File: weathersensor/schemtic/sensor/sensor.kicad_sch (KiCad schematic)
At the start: 1 part

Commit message: backup
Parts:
- removed J?: Conn_Coaxial, symbol Connector:Conn_Coaxial
- added C1, C2, C? (x3): 1.0u, symbol Device:C_Small
- added C3: 10u, symbol Device:C_Small
- added C? (x2): C_Polarized, symbol Device:C_Polarized
- added D1: BAT60A, Diode_SMD:D_SOD-323, symbol Diode:BAT60A
- added D2, D? (x2): LED, symbol Device:LED
- added D? (x2): D_Schottky, symbol Device:D_Schottky
- added IC?: CN3791, SSOP10, symbol CN3791:CN3791
- added J1: Conn_01x04_Male, Connector_JST:JST_XH_B4B-XH-AM_1x04_P2.50mm_Vertical, symbol Connector:Conn_01x04_Male
- added J2: Conn_01x02_Male, Connector_JST:JST_PH_B2B-PH-K_1x02_P2.00mm_Vertical, symbol Connector:Conn_01x02_Male
- added J3: Conn_01x02_Male, Connector_JST:JST_XH_B2B-XH-AM_1x02_P2.50mm_Vertical, symbol Connector:Conn_01x02_Male
- added L?: INDUCTOR, symbol pspice:INDUCTOR
- added Q1: IRLML6401, Package_TO_SOT_SMD:SOT-23, symbol Transistor_FET:IRLML6401
- added R1, R2: 10k, symbol Device:R
- added R3, R? (x4): 1k, symbol Device:R
- added U1: XC6220B331MR, Package_TO_SOT_SMD:SOT-23-5, symbol Regulator_Linear:XC6220B331MR
- added U2: CH340C, Package_SO:SOIC-16_3.9x9.9mm_P1.27mm, symbol Interface_USB:CH340C
- added U3: MS5611-01BA, Package_LGA:LGA-8_3x5mm_P1.25mm, symbol Sensor_Pressure:MS5611-01BA
- added U4: RFM95W-868S2, RF_Module:HOPERF_RFM9XW_THT, symbol RF_Module:RFM95W-868S2
- added U6: MAX17048G, SON50P200X200X80-9N, symbol MAX17048G:MAX17048G
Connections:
- new net: C1.1, D1.1 (K), Q1.2 (S), R2.1, U1.1 (VIN)
- new net: R2.2, U1.3 (CE)
- new net: D2.2 (A), R3.2
- new net: U3.4 (CSB), U3.5 (CSB)
- new net +3.3V: C2.1, C3.1, R3.1, U1.5 (VOUT)
- new net GND: C1.2, C2.2, C3.2, D2.1 (K), R1.2, U1.2 (GND)
- new net VSS: C?.1
- new net V_BAT: Q1.3 (D)
- new net V_USB: D1.2 (A), Q1.1 (G), R1.1
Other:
- note added: "Power Supply"

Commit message: Start commit message
21.03.2023
	- create and pcb for weathersensor

22.02.2023
	- add schematic and pcb for mqtt_wlan_bridge
	- remove old from git repo

	TODO:
	- create schematic and pcb for weathersensor
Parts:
- removed D? (x2): LED, symbol Device:LED
- removed R?: 1k, symbol Device:R
- added C11, C13, C8: 100n, Capacitor_SMD:C_1206_3216Metric, symbol Device:C_Small
- added C12: 1u, Capacitor_SMD:C_1206_3216Metric, symbol Device:C_Small
- added C7: 22n, Capacitor_SMD:C_1206_3216Metric, symbol Device:C_Small
- added IC2: DW01A, DW01A:SOT23-6, symbol DW01A:DW01A
- added J4: ANT, Connector_Coaxial:SMA_Amphenol_901-144_Vertical, symbol Connector:Conn_Coaxial
- added P1: USB_C_Plug_USB2.0, Connector_USB:USB_C_Receptacle_HRO_TYPE-C-31-M-12, symbol Connector:USB_C_Plug_USB2.0
- added Q2: AO3401A, Package_TO_SOT_SMD:SOT-23, symbol Transistor_FET:AO3401A
- added Q3: FS8205, FS8205:SOT95P280X145-6N, symbol FS8205:FS8205
- added Q4, Q5: BSS138, Package_TO_SOT_SMD:SOT-23, symbol Transistor_FET:BSS138
- added R10: 1k, Resistor_SMD:R_1206_3216Metric, symbol Device:R
- added R11, R4: 5k1, Resistor_SMD:R_1206_3216Metric, symbol Device:R
- added R12, R13: 10k, Resistor_SMD:R_1206_3216Metric, symbol Device:R
- added R7: 178k, Resistor_SMD:R_1206_3216Metric, symbol Device:R
- added R8: 100, Resistor_SMD:R_1206_3216Metric, symbol Device:R
- C1, C2: footprint (none) -> Capacitor_SMD:C_1206_3216Metric; Feld4 (none) -> C107185
- C10: renamed from C?; value 1.0u -> 220n; footprint (none) -> Capacitor_SMD:C_1206_3216Metric; Feld4 (none) -> C377090
- C3: footprint (none) -> Capacitor_SMD:C_1206_3216Metric; Feld4 (none) -> C92797
- C4, C9: renamed from C?; value C_Polarized -> 47u/16V; footprint (none) -> Capacitor_SMD:CP_Elec_5x5.3; Feld4 (none) -> C134798
- C5: renamed from C?; value 1.0u -> 10n; footprint (none) -> Capacitor_SMD:C_1206_3216Metric; Feld4 (none) -> C1846
- C6: renamed from C?; value 1.0u -> 100n; footprint (none) -> Capacitor_SMD:C_1206_3216Metric; Feld4 (none) -> C377067
- D1: Feld4 (none) -> C117485
- D2: footprint (none) -> LED_SMD:LED_1206_3216Metric; Feld4 (none) -> C84273
- D5, D6: renamed from D?; value D_Schottky -> SSB43L; footprint (none) -> Diode_SMD:D_SMB; Feld4 (none) -> C222519
- IC1: renamed from IC?; footprint SSOP10 -> CN3791:SSOP10; Feld4 (none) -> C154992
- J1: value Conn_01x04_Male -> I2C
- J2: value Conn_01x02_Male -> PANEL; footprint Connector_JST:JST_PH_B2B-PH-K_1x02_P2.00mm_Vertical -> TerminalBlock:TerminalBlock_Altech_AK300-2_P5.00mm
- J3: value Conn_01x02_Male -> BAT
- L1: renamed from L?; value INDUCTOR -> 82u; footprint (none) -> Inductor_SMD:L_12x12mm_H8mm; Feld4 (none) -> C504035
- Q1: Feld4 (none) -> C347501
- R1, R2: footprint (none) -> Resistor_SMD:R_1206_3216Metric; Feld4 (none) -> C118075
- R3: footprint (none) -> Resistor_SMD:R_1206_3216Metric; Feld4 (none) -> C4410
- R5: renamed from R?; value 1k -> 120; footprint (none) -> Resistor_SMD:R_1206_3216Metric; Feld4 (none) -> C114928
- R6: renamed from R?; value 1k -> 22k; footprint (none) -> Resistor_SMD:R_1206_3216Metric; Feld4 (none) -> C25830
- R9: renamed from R?; value 1k -> 0.05; footprint (none) -> Resistor_SMD:R_1206_3216Metric; Feld4 (none) -> C149662
- U1: Feld4 (none) -> C86534
- U2: Feld4 (none) -> C84681
- U3: Feld4 (none) -> C37148
- U6: footprint SON50P200X200X80-9N -> MAX17048G:SON50P200X200X80-9N; Feld4 (none) -> C2682616
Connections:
- net +3.3V: now also J1.1 (Pin_1), U2.16 (VCC), U2.4 (V3), U3.1 (VDD), U3.2 (PS), U4.13 (3.3V), C11.1, C13.1, R12.2, R13.2
- net GND: now also C1.1, C10.2, C4.2, C5.2, C9.2, D6.2 (A), IC1.2 (GND), J1.2 (Pin_2), J2.2 (Pin_2), J3.2 (Pin_2), R6.1, U2.1 (GND), U3.3 (GND), U3.4 (CSB), U3.5 (CSB), U4.1 (GND), U4.10 (GND), U4.8 (GND), U6.1 (CTG), U6.4 (GND), U6.6 (QSTRT), C11.2, C12.2, C13.2, C7.2, C8.2, IC2.6 (GND), J4.2 (Ext), P1.A1 (GND), P1.A12 (GND), P1.B1 (GND), P1.B12 (GND), P1.S1 (SHIELD), Q3.3, R10.1, R11.1, R4.1; no longer C1.2
- net VSS: now also C4.1, C5.1, IC1.9 (VCC), J2.1 (Pin_1), Q2.3 (D), Q3.1, R7.2
- net V_BAT: now also C10.1, C9.1, J3.1 (Pin_1), R9.2, U6.2 (CELL), U6.3 (VDD), R8.2
- net V_USB: now also P1.A4 (VBUS), P1.A9 (VBUS), P1.B4 (VBUS), P1.B9 (VBUS)
- net SCL: now reaches J1.3 (Pin_3)
- net SCL: now also U3.8 (SCLK), U6.7 (SCL), R12.1
- net SDA: now reaches J1.4 (Pin_4)
- net SDA: now also U3.7 (SDI/SDA), U6.8 (SDA), R13.1
- net at D1.1 (K), Q1.2 (S), R2.1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: now also C1.2; no longer C1.1
- net at C6.2: now also IC1.1 (VG)
- net at R5.1: now also IC1.5 (COM)
- net at R5.2: now also C7.1
- net RFM_DI0: now reaches U4.14 (DIO0)
- net MISO: now reaches U4.2 (MISO)
- net MOSI: now reaches U4.3 (MOSI)
- net SCK: now reaches U4.4 (SCK)
- net RFM_SS: now reaches U4.5 (NSS)
- net RFM_RESET: now reaches U4.6 (RESET)
- net RF_ANT: now reaches U4.9 (ANT)
- net RF_ANT: now also J4.1 (In)
- net at R9.1: now also IC1.7 (BAT), L1.2
- net at D6.1 (K): now also D5.1 (K), IC1.8 (CSP), L1.1
- net at R6.2: now also IC1.6 (MPPT), R7.1
- net at IC1.10 (DRV): now also Q2.1 (G)
- net CHARGE: now reaches IC1.3 (CHRG)
- net CRG_DONE: now reaches IC1.4 (DONE)
- net at U2.13 (~{DTR}): now also Q4.1 (G), Q5.2 (S)
- net at U2.14 (~{RTS}): now also Q4.2 (S), Q5.1 (G)
- net ESP32_RX: now reaches U2.2 (TXD)
- net ESP32_TX: now reaches U2.3 (RXD)
- net at U2.5 (UD+): now also P1.A6 (D+)
- net at U2.6 (UD-): now also P1.A7 (D-)
- net at D5.2 (A): now also Q2.2 (S)
- net ALERT: now reaches U6.5 (~{ALERT})
- new net: IC2.2 (CS), R10.2
- new net: C8.1, IC2.5 (VCC), R8.1
- new net: Q3.2, Q3.5
- new net: IC2.3 (OC), Q3.4
- new net: IC2.1 (OD), Q3.6
- new net: P1.A5 (CC), R11.2
- new net: P1.B5 (VCONN), R4.2
- new net ESP32_EN: C12.1, Q4.3 (D)
- new net ESP32_IO0: Q5.3 (D)
- no-connect marks 0 -> 14
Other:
- added sheet ESP32_WROOM (untitled.kicad_sch)
- note added: "Barometer"
- note added: "Fuel Gauge"
- note added: "I2C Address 0x77"
- note added: "LiPo Proctection"
- note added: "LiPo-Charger"
- title: (none) -> Ambiente Sensor
- moved on the sheet: C1, C10, C4, C5, C6, C9, D5, D6, IC1, J1, J2, J3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

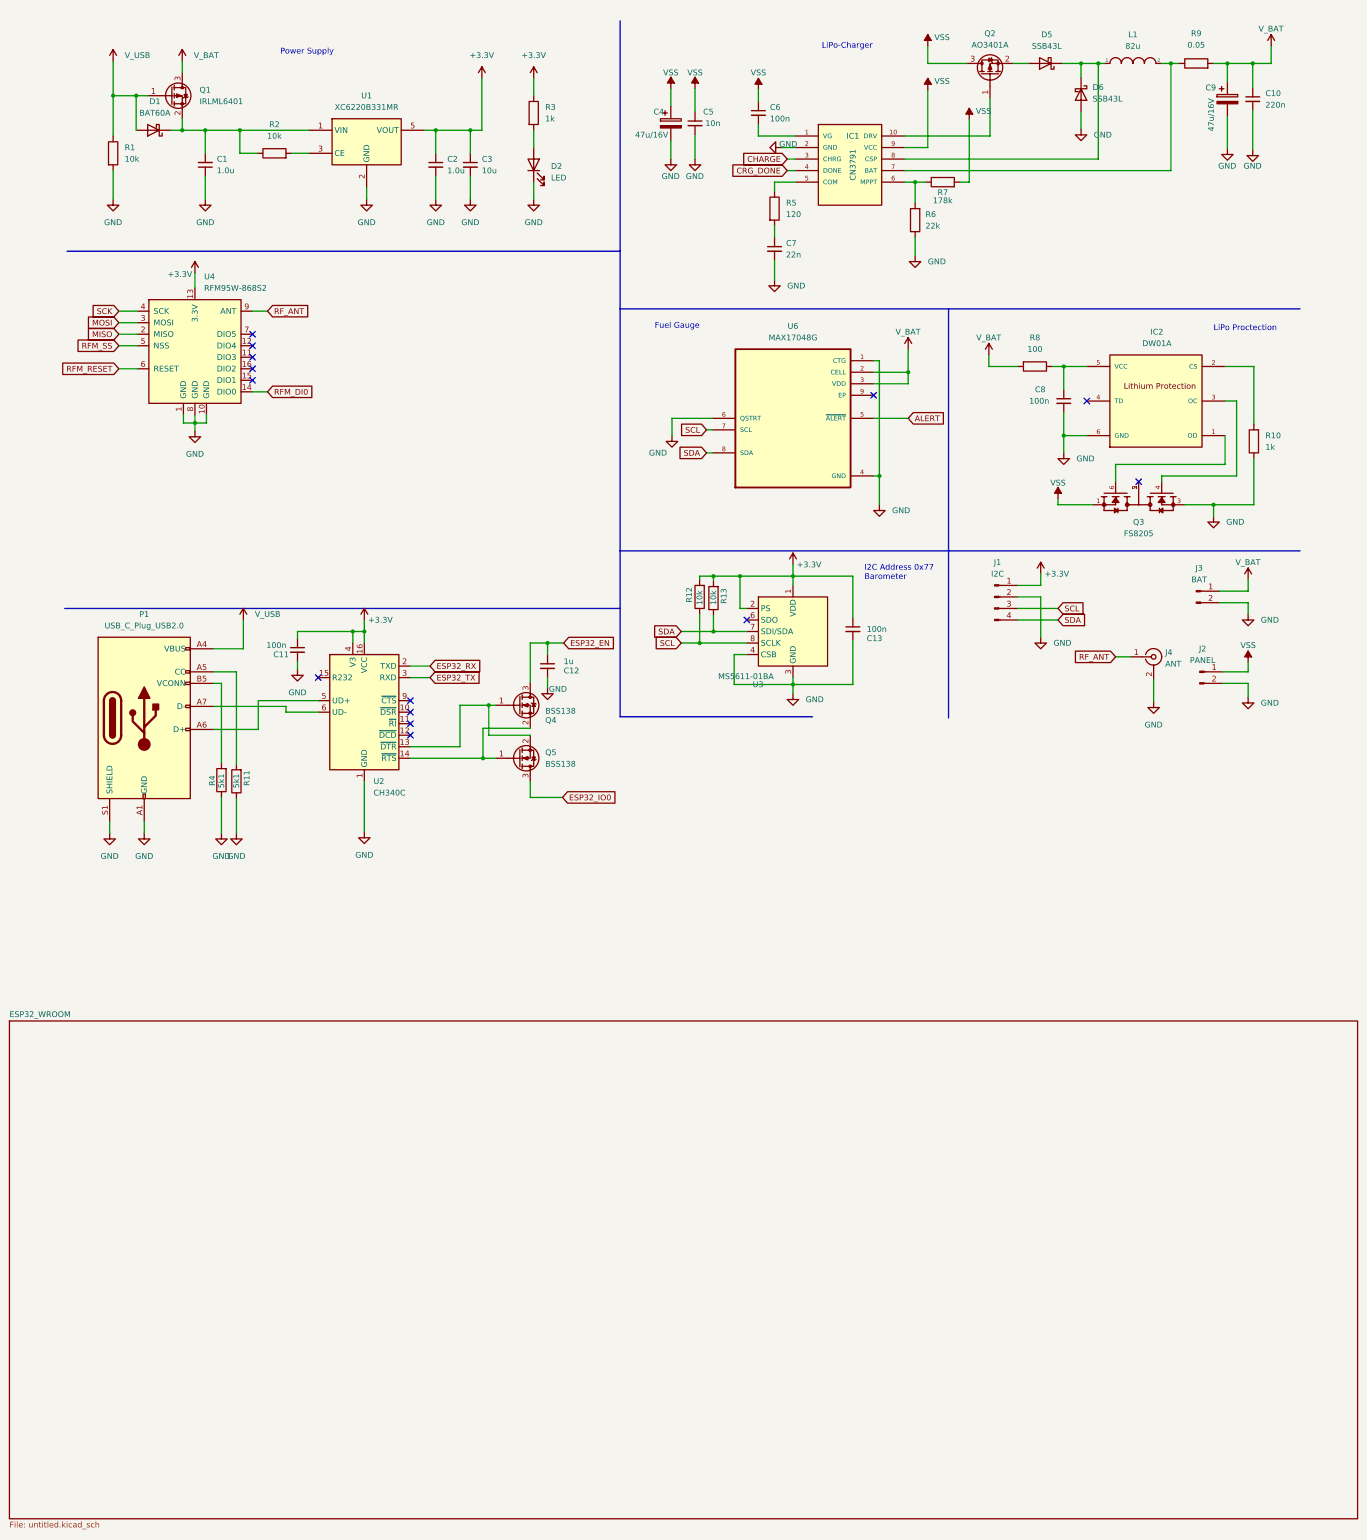
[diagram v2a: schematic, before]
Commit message: Changes in Source Code:
    use the interal ADC for measure battery and panel voltage
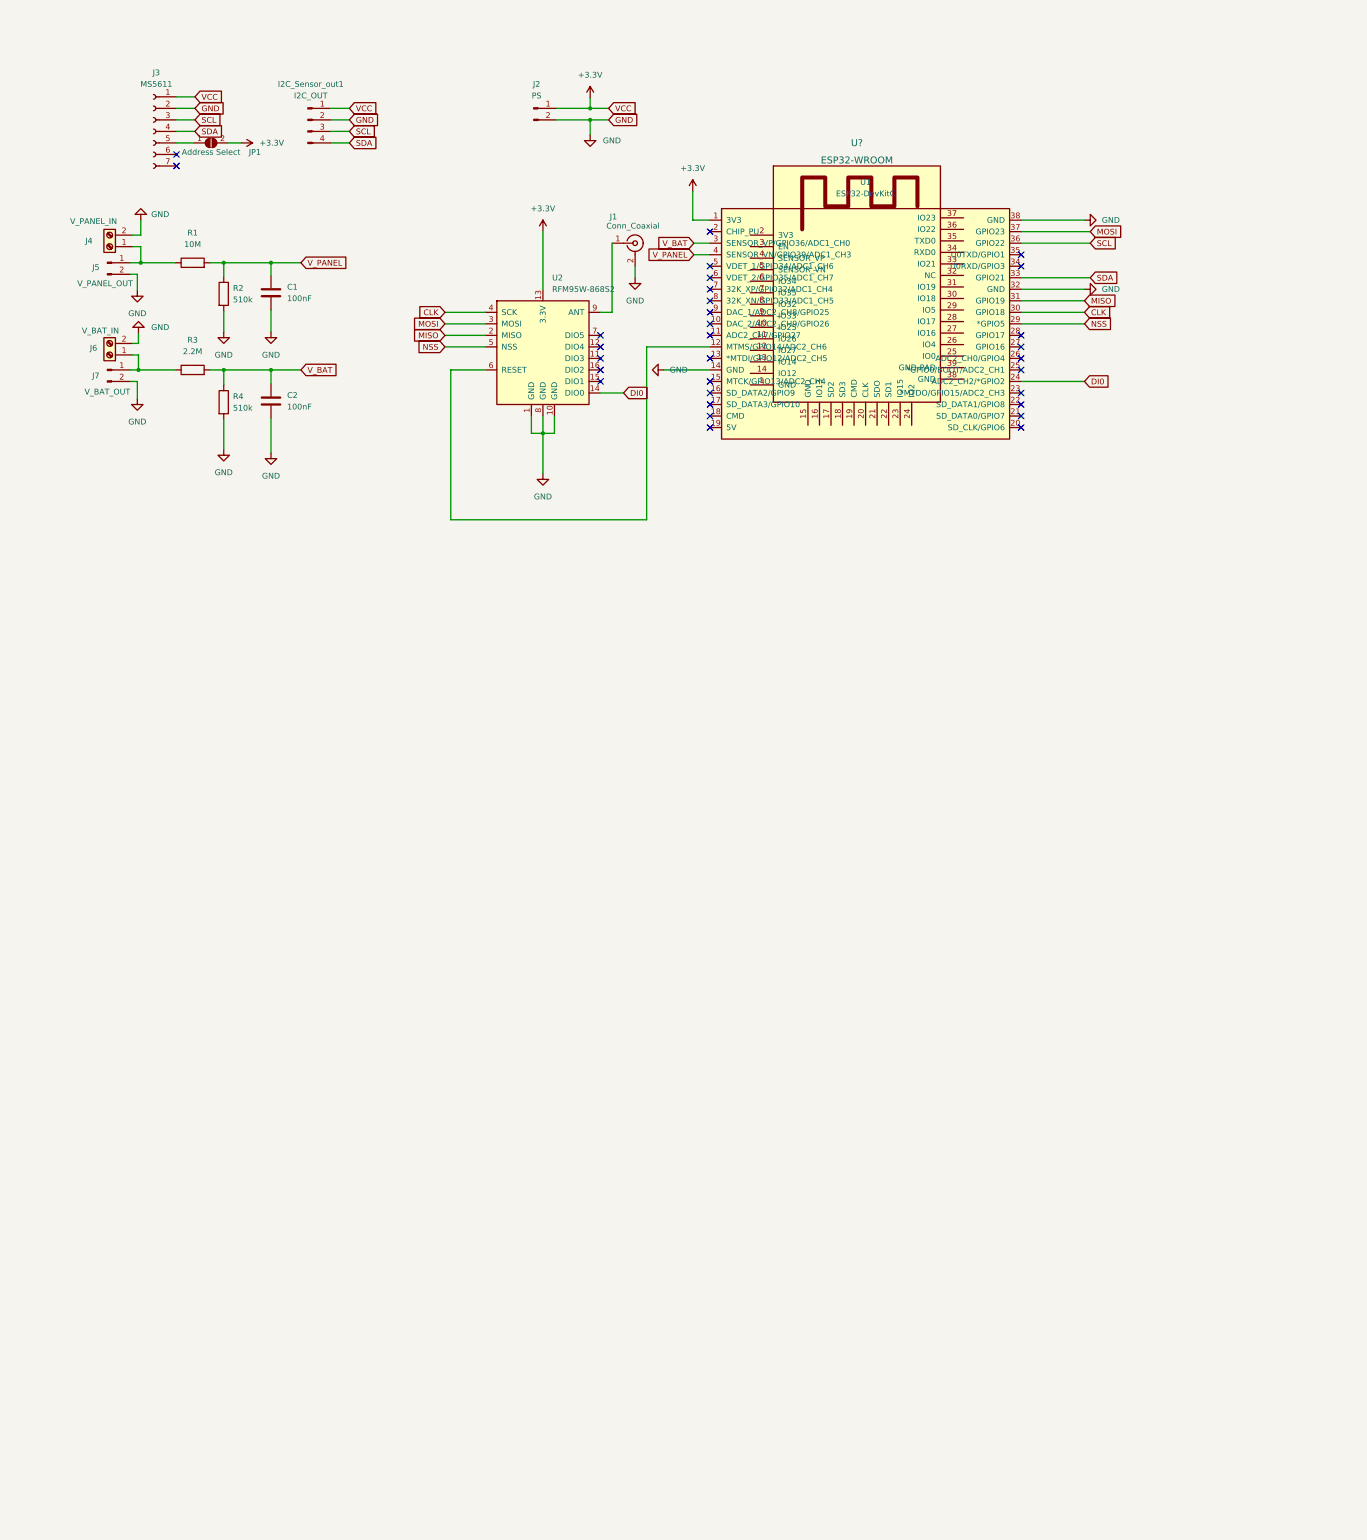
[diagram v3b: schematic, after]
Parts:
- removed C1, C2: 1.0u, Capacitor_SMD:C_1206_3216Metric, symbol Device:C_Small
- removed C10: 220n, Capacitor_SMD:C_1206_3216Metric, symbol Device:C_Small
- removed C11, C13, C6, C8: 100n, Capacitor_SMD:C_1206_3216Metric, symbol Device:C_Small
- removed C12: 1u, Capacitor_SMD:C_1206_3216Metric, symbol Device:C_Small
- removed C3: 10u, Capacitor_SMD:C_1206_3216Metric, symbol Device:C_Small
- removed C4, C9: 47u/16V, Capacitor_SMD:CP_Elec_5x5.3, symbol Device:C_Polarized
- removed C5: 10n, Capacitor_SMD:C_1206_3216Metric, symbol Device:C_Small
- removed C7: 22n, Capacitor_SMD:C_1206_3216Metric, symbol Device:C_Small
- removed D1: BAT60A, Diode_SMD:D_SOD-323, symbol Diode:BAT60A
- removed D2: LED, LED_SMD:LED_1206_3216Metric, symbol Device:LED
- removed D5, D6: SSB43L, Diode_SMD:D_SMB, symbol Device:D_Schottky
- removed IC1: CN3791, CN3791:SSOP10, symbol CN3791:CN3791
- removed IC2: DW01A, DW01A:SOT23-6, symbol DW01A:DW01A
- removed J1: I2C, Connector_JST:JST_XH_B4B-XH-AM_1x04_P2.50mm_Vertical, symbol Connector:Conn_01x04_Male
- removed J3: BAT, Connector_JST:JST_XH_B2B-XH-AM_1x02_P2.50mm_Vertical, symbol Connector:Conn_01x02_Male
- removed J4: ANT, Connector_Coaxial:SMA_Amphenol_901-144_Vertical, symbol Connector:Conn_Coaxial
- removed L1: 82u, Inductor_SMD:L_12x12mm_H8mm, symbol pspice:INDUCTOR
- removed P1: USB_C_Plug_USB2.0, Connector_USB:USB_C_Receptacle_HRO_TYPE-C-31-M-12, symbol Connector:USB_C_Plug_USB2.0
- removed Q1: IRLML6401, Package_TO_SOT_SMD:SOT-23, symbol Transistor_FET:IRLML6401
- removed Q2: AO3401A, Package_TO_SOT_SMD:SOT-23, symbol Transistor_FET:AO3401A
- removed Q3: FS8205, FS8205:SOT95P280X145-6N, symbol FS8205:FS8205
- removed Q4, Q5: BSS138, Package_TO_SOT_SMD:SOT-23, symbol Transistor_FET:BSS138
- removed R10: 1k, Resistor_SMD:R_1206_3216Metric, symbol Device:R
- removed R11: 5k1, Resistor_SMD:R_1206_3216Metric, symbol Device:R
- removed R12, R13: 10k, Resistor_SMD:R_1206_3216Metric, symbol Device:R
- removed R5: 120, Resistor_SMD:R_1206_3216Metric, symbol Device:R
- removed R6: 22k, Resistor_SMD:R_1206_3216Metric, symbol Device:R
- removed R7: 178k, Resistor_SMD:R_1206_3216Metric, symbol Device:R
- removed R8: 100, Resistor_SMD:R_1206_3216Metric, symbol Device:R
- removed R9: 0.05, Resistor_SMD:R_1206_3216Metric, symbol Device:R
- removed U1: XC6220B331MR, Package_TO_SOT_SMD:SOT-23-5, symbol Regulator_Linear:XC6220B331MR
- removed U2: CH340C, Package_SO:SOIC-16_3.9x9.9mm_P1.27mm, symbol Interface_USB:CH340C
- removed U3: MS5611-01BA, Package_LGA:LGA-8_3x5mm_P1.25mm, symbol Sensor_Pressure:MS5611-01BA
- removed U4: RFM95W-868S2, RF_Module:HOPERF_RFM9XW_THT, symbol RF_Module:RFM95W-868S2
- removed U6: MAX17048G, MAX17048G:SON50P200X200X80-9N, symbol MAX17048G:MAX17048G
- added C1, C2: 100nF, Capacitor_THT:C_Disc_D3.0mm_W1.6mm_P2.50mm, symbol Device:C
- added I2C_Sensor_out1: I2C_OUT, Connector_JST:JST_XH_B4B-XH-AM_1x04_P2.50mm_Vertical, symbol Connector:Conn_01x04_Male
- added J1: Conn_Coaxial, Connector_Coaxial:SMA_Amphenol_132203-12_Horizontal, symbol Connector:Conn_Coaxial
- added J3: MS5611, Connector_PinHeader_2.54mm:PinHeader_1x07_P2.54mm_Vertical, symbol Connector:Conn_01x07_Female
- added J4: V_PANEL_IN, TerminalBlock_RND:TerminalBlock_RND_205-00012_1x02_P5.00mm_Horizontal, symbol Connector:Screw_Terminal_01x02
- added J5: V_PANEL_OUT, Connector_PinHeader_2.54mm:PinHeader_1x02_P2.54mm_Vertical, symbol Connector:Conn_01x02_Male
- added J6: V_BAT_IN, TerminalBlock_RND:TerminalBlock_RND_205-00012_1x02_P5.00mm_Horizontal, symbol Connector:Screw_Terminal_01x02
- added J7: V_BAT_OUT, Connector_PinHeader_2.54mm:PinHeader_1x02_P2.54mm_Vertical, symbol Connector:Conn_01x02_Male
- added JP1: Address Select, Jumper:SolderJumper-2_P1.3mm_Open_RoundedPad1.0x1.5mm, symbol Jumper:SolderJumper_2_Open
- added U1: ESP32-DevKitC, ESP32-DEVKITC-32D:MODULE_ESP32-DEVKITC-32D, symbol Espressif:ESP32-DevKitC
- added U2: RFM95W-868S2, RF_Module:HOPERF_RFM9XW_THT, symbol RF_Module:RFM95W-868S2
- added U?: ESP32-WROOM, ESP32-footprints-Lib:ESP32, symbol ESP32-footprints-Shem-Lib:ESP32-WROOM
- J2: value PANEL -> PS; footprint TerminalBlock:TerminalBlock_Altech_AK300-2_P5.00mm -> Connector_PinHeader_2.54mm:PinHeader_1x02_P2.54mm_Vertical
- R1: value 10k -> 10M; footprint Resistor_SMD:R_1206_3216Metric -> Resistor_THT:R_Axial_DIN0204_L3.6mm_D1.6mm_P5.08mm_Horizontal; Feld4 C118075 -> (none)
- R2: value 10k -> 510k; footprint Resistor_SMD:R_1206_3216Metric -> Resistor_THT:R_Axial_DIN0204_L3.6mm_D1.6mm_P5.08mm_Horizontal; Feld4 C118075 -> (none)
- R3: value 1k -> 2.2M; footprint Resistor_SMD:R_1206_3216Metric -> Resistor_THT:R_Axial_DIN0204_L3.6mm_D1.6mm_P5.08mm_Horizontal; Feld4 C4410 -> (none)
- R4: value 5k1 -> 510k; footprint Resistor_SMD:R_1206_3216Metric -> Resistor_THT:R_Axial_DIN0204_L3.6mm_D1.6mm_P5.08mm_Horizontal; Feld4 C104846 -> (none)
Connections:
- net VSS is gone; now on net +3.3V: J2.1 (Pin_1)
- net +3.3V: now also I2C_Sensor_out1.1 (Pin_1), J3.1 (Pin_1), JP1.2 (B), U1.1 (3V3), U2.13 (3.3V); no longer R3.1
- net GND: now also R2.2, R4.2, C1.2, C2.2, I2C_Sensor_out1.2 (Pin_2), J1.2 (Ext), J3.2 (Pin_2), J4.2 (Pin_2), J5.2 (Pin_2), J6.2 (Pin_2), J7.2 (Pin_2), U1.14 (GND), U1.32 (GND), U1.38 (GND), U2.1 (GND), U2.10 (GND), U2.8 (GND); no longer R1.2, R4.1
- net MISO: now also U1.31 (GPIO19), U2.2 (MISO)
- net MOSI: now also U1.37 (GPIO23), U2.3 (MOSI)
- net SCL: now also I2C_Sensor_out1.3 (Pin_3), J3.3 (Pin_3), U1.36 (GPIO22)
- net SDA: now also I2C_Sensor_out1.4 (Pin_4), J3.4 (Pin_4), U1.33 (GPIO21)
- net V_BAT: now also R3.2, R4.1, C2.1, U1.3 (SENSOR_VP/GPIO36/ADC1_CH0)
- net V_PANEL: now reaches R2.1
- net V_PANEL: now also R1.2, C1.1, U1.4 (SENSOR_VN/GPIO39/ADC1_CH3)
- net V_USB: no longer names the net of R1.1
- net V_USB: now also J4.1 (Pin_1), J5.1 (Pin_1)
- new net: J3.5 (Pin_5), JP1.1 (A)
- new net: J6.1 (Pin_1), J7.1 (Pin_1), R3.1
- new net: J1.1 (In), U2.9 (ANT)
- new net: U1.12 (MTMS/GPIO14/ADC2_CH6), U2.6 (RESET)
- new net CLK: U1.30 (GPIO18), U2.4 (SCK)
- new net DI0: U1.24 (ADC2_CH2/*GPIO2), U2.14 (DIO0)
- new net NSS: U1.29 (*GPIO5), U2.5 (NSS)
- no-connect marks 14 -> 31
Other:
- removed sheet ESP32_WROOM
- note removed: "Barometer"
- note removed: "Fuel Gauge"
- note removed: "I2C Address 0x77"
- note removed: "LiPo Proctection"
- note removed: "LiPo-Charger"
- note removed: "Power Supply"
